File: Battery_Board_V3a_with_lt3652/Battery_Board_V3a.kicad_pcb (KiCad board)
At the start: 4 copper layers, 88 x 94.5 mm, 204 parts, among them IC2 PCT2075DP,118, IC3 RP2040_QFN56, IC4 LT3652IMSE#PBF, J1 Bypass, J10 Jetson, J11 BM04B-SRSS-TB(LF)(SN), J14 Solar, J15 FC, J16 I2C Multiplexer Breakout, J17 ISS Foot, J18 Screw_Terminal_01x02, J19 BM04B-SRSS-TB(LF)(SN), J2 Heater, J20 CAN1, J21 BM04B-SRSS-TB(LF)(SN), J22 CAN2, J23 Conn_ARM_JTAG_SWD_10, J24 USB_B_Micro, J25 Life Makes Lemonade, J26 BM04B-SRSS-TB(LF)(SN), J27 I2C0 Breakout, J3 BURN, J4 CHARGE, J5 Foot0, J6 Foot1, J7 Foot2, J8 Foot3, J9 RBF, K1 APAN3105, Q1 IRF7458, Q10 IRLML2803, Q11 NDS8434, Q2 IRF7458, Q3 MBT2222ADW1T1, Q4 MMBT2222AT, Q5 MBT2222ADW1T1, Q6 IRLML2803, Q7 IRLML2803, Q8 NDS8434, Q9 NDS8434, SW1 KMR2, SW2 KMR2, U1 R5460N208AA, U10 TLVH431 DBZ SOT-23, U11 MCP25625-E/ML, U12 INA219AxD, U13 MAX706RESA, U14 INA219AxD, U2 1049, U3 TPS54226PWPRPWP14_2P31X2P46-L, U4 1049, U5 TPS54226PWPRPWP14_2P31X2P46-L, U6 TPS7A4501DCQT, U7 ADS1015IDGS, U8 W25Q128JV, U9 AD8495, Y1 Crystal_GND24, Y2 Crystal_GND24

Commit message: Footprint Changes
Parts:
- C3, C4: footprint Capacitor_SMD:C_1210_3225Metric -> Capacitor_SMD:C_1206_3216Metric
- D4, D7: value D_Schottky -> DFLS130L-7; footprint Diode_SMD:D_SMB -> Diode_SMD:D_PowerDI-123
- moved C4 1.48 mm to (153.3, 88.0)
- moved C3 1.38 mm to (158.4, 89.4)
- moved D7 0.99 mm to (167.9, 109.0)
- moved D4 0.55 mm to (175.1, 121.4)
- moved R65 0.11 mm to (191.4, 127.4), turned to 0 degrees
- moved D1 0.06 mm to (120.2, 70.2)
- moved D9 0.05 mm to (171.7, 96.7)
- moved D6 0.05 mm to (171.7, 99.4)
- turned R64 to 180 degrees
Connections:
- C39 pad 2: Net-(IC4-BOOST) -> Net-(D6-K)
- IC4 pad 11: Net-(IC4-BOOST) -> Net-(D6-K)
- K1 pad C2: Net-(Q4-C) -> Net-(D1-A)
- Q4 pad 3: Net-(Q4-C) -> Net-(D1-A)
- R62 pad 1: Chassis Ground -> GND
- R62 pad 2: GND -> Chassis Ground
- R63 pad 1: Chassis Ground -> GND
- R63 pad 2: GND -> Chassis Ground
- R64 pad 1: Chassis Ground -> GND
- R64 pad 2: GND -> Chassis Ground
- R65 pad 1: Chassis Ground -> GND
- R65 pad 2: GND -> Chassis Ground
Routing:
- net Net-(Q4-C): track 18.1 -> 0.00 mm
- net Net-(D1-A): track 0.00 -> 18.1 mm
- net Net-(IC4-BOOST): track 10.7 -> 0.00 mm
- net Net-(D6-K): track 0.00 -> 10.7 mm
- net Chassis Ground: track 9.91 -> 13.0 mm, vias 0 -> 2
- net GND: track 310.1 -> 311.6 mm, vias 61 -> 59
- net VBUSP: track 172.6 -> 174.0 mm
- net VSOLAR_I: track 7.77 -> 8.95 mm
- net +3V3: vias 22 -> 25

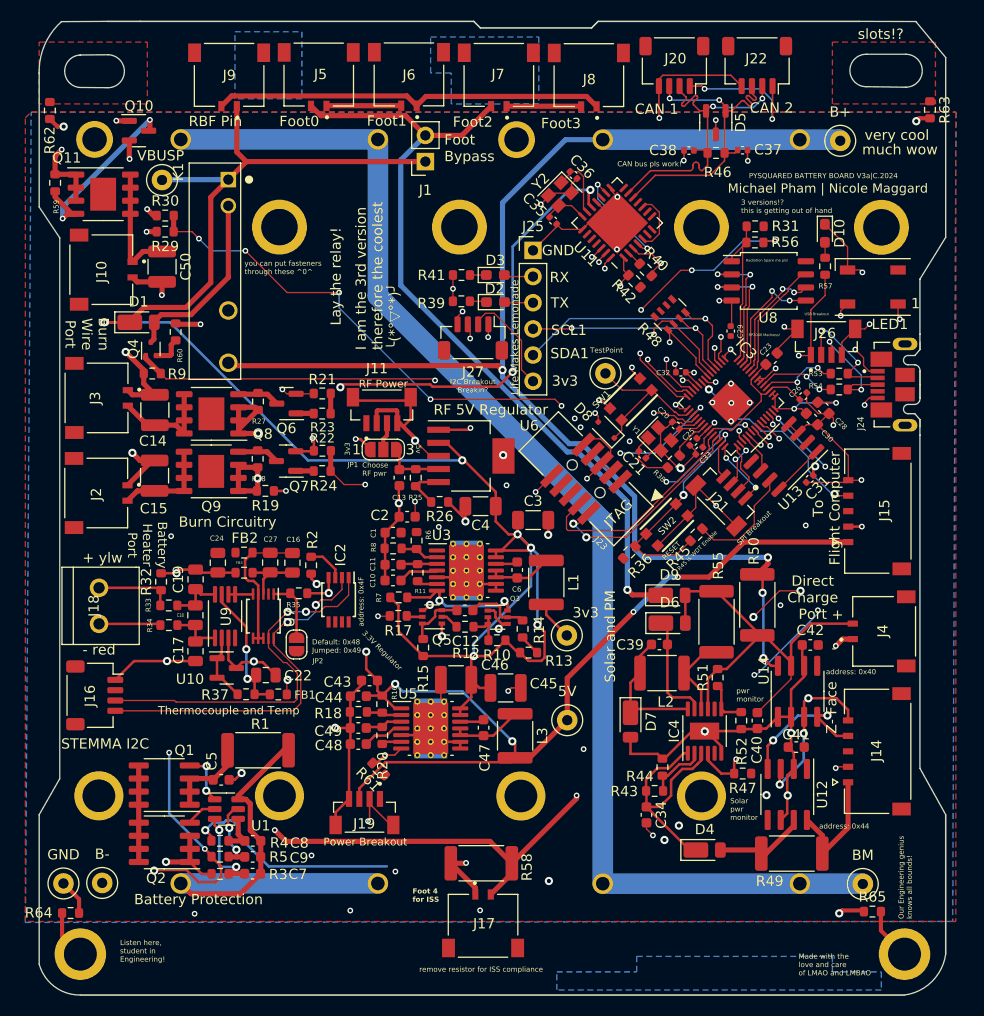
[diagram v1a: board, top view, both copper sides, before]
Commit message: [MAJOR ISSUE] Fixed Burn_Enable Issue
MAJOR ISSUE:
Burn Wire Circuit does not work on V3a due to mislabeled schematic nets. uController had Enable_Burn rather than ENAB_Burn. Change was make so not uController connects to the ENAB_Burn
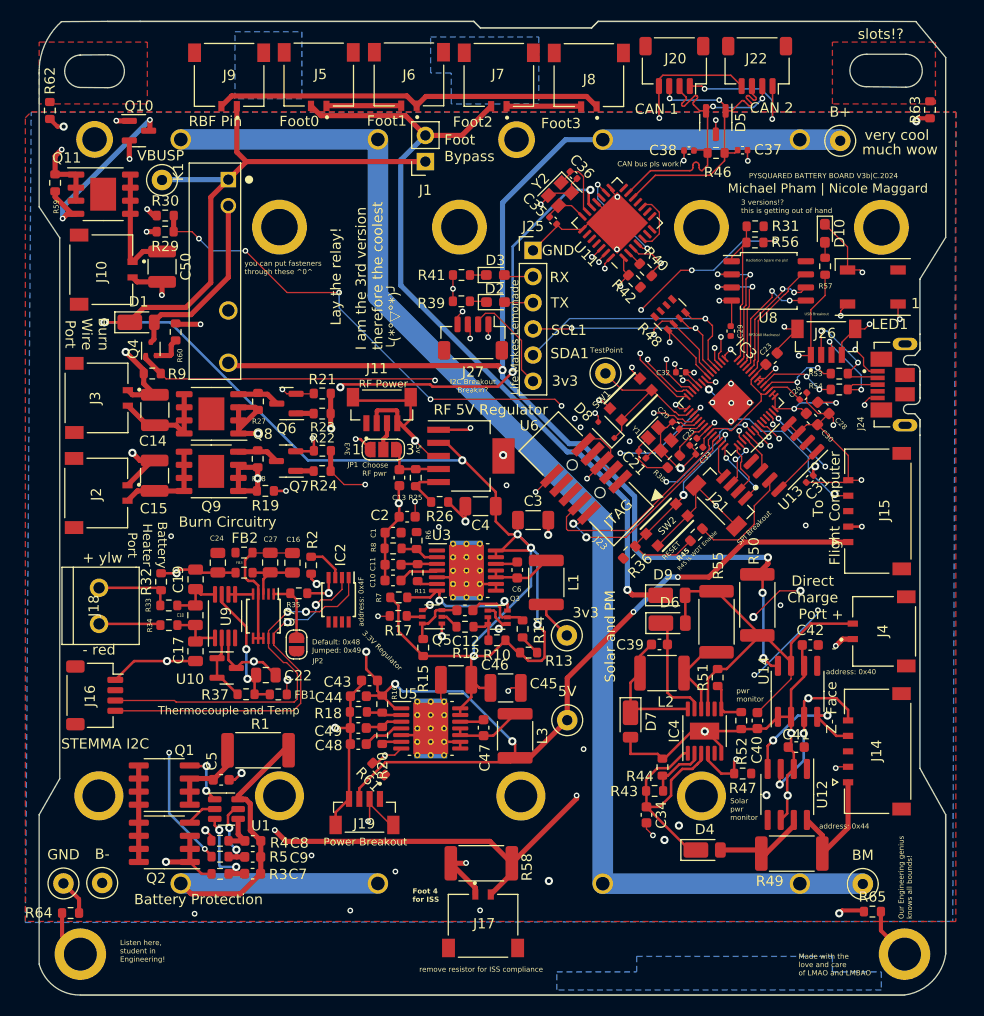
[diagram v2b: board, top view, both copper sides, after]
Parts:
- turned R62 to 90 degrees
- turned R63 to 90 degrees
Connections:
- IC3 pad 8: ENABLE_BURN -> ENAB_BURN
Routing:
- net ENAB_BURN: track 1.95 -> 43.9 mm, vias 0 -> 2
- net BM: track 188.1 -> 167.7 mm
- net PACK+: track 224.9 -> 215.3 mm, vias 9 -> 8
- net Chassis Ground: track 13.0 -> 9.91 mm, vias 2 -> 0
- net GND: track 311.6 -> 314.7 mm, vias 59 -> 61
- net ENABLE_BURN: track 1.24 -> 0.00 mm, vias 1 -> 0
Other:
- board text added: "PYSQUARED BATTERY BOARD V3b|C.2024"
- board text removed: "PYSQUARED BATTERY BOARD V3a|C.2024"
